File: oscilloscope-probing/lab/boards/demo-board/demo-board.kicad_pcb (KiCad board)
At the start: 4 copper layers, 12.8 x 6.5 mm, 265 parts, among them J1 CONN_01X03, J10 SMA-J-P-H-ST-EM1, J11 TESTCLIP, J12 TESTCLIP, J13 TESTCLIP, J14 USB_C_Receptacle_USB2.0, J15 TESTCLIP, J16 SMA-J-P-H-ST-EM1, J17 SMA-J-P-H-ST-EM1, J18 SMA-J-P-H-ST-EM1, J19 SMA-J-P-H-ST-EM1, J2 CORTEX_DEBUG_ETM, J3 XILINX_JTAG, J4 CORTEX_DEBUG_ETM, J5 DISPLAY, J6 CONN_01X06, J7 SMA-J-P-H-ST-EM1, J8 SMA-J-P-H-ST-EM1, J9 SMA-J-P-H-ST-EM1, Q1 SSM6N58NU, SW1 SWITCH, SW2 SWITCH, SW3 SWITCH, SW4 SWITCH, SW5 SWITCH, SW6 SWITCH, SW7 SWITCH, U1 FT234XD, U10 19-C47/RSGHBHC-5V01/2T, U11 19-C47/RSGHBHC-5V01/2T, U12 19-C47/RSGHBHC-5V01/2T, U13 19-C47/RSGHBHC-5V01/2T, U2 STM32L431-QFN48, U26 74LVC1T45, U3 LTC3374A, U39 NCP45525IMNTWG-H, U4 XC7A35T-2FGG484I, U5 STM32H750XBH6, U6 ECS-1612MV-250-CN, U7 ECS-1612MV-250-CN, U8 S25FL064LABMFI013, U9 SIT9121AI-2BF-XXS156.250000G

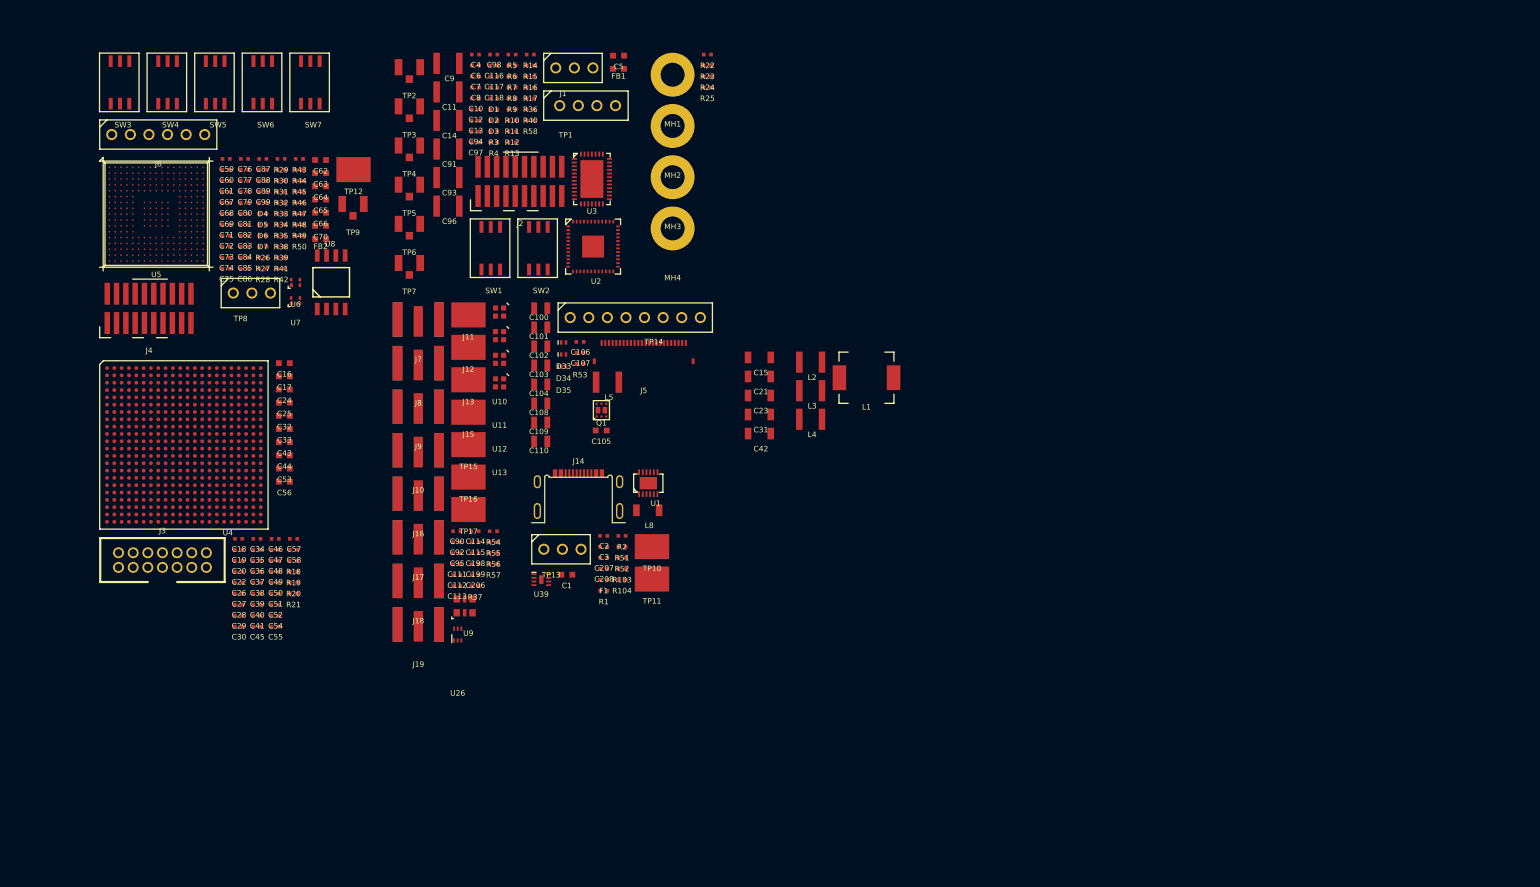
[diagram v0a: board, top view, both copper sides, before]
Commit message: Continued demo board layout
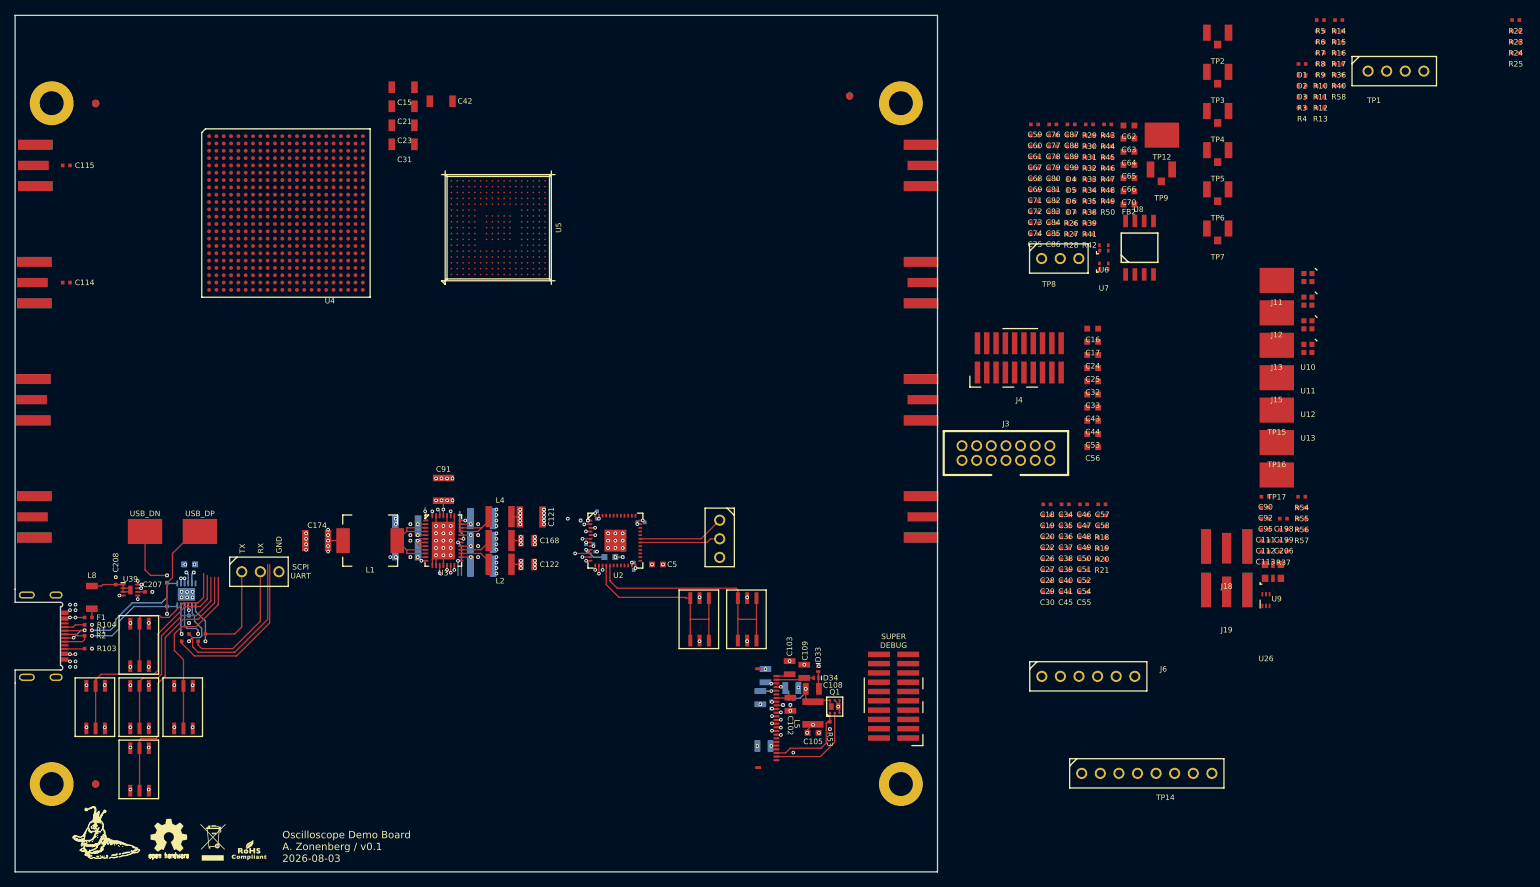
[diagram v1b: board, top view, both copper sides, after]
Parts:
- added C119: 0.47 uF, azonenberg_pcb:EIA_0402_CAP_NOSILK, F.Cu at (80.5, 98.0)
- added C120: 0.47 uF, azonenberg_pcb:EIA_0402_CAP_NOSILK, F.Cu at (80.5, 95.8)
- added C121: 47 uF, azonenberg_pcb:EIA_1210_CAP_NOSILK, F.Cu at (96.5, 92.5)
- added C122: 22 uF, azonenberg_pcb:EIA_0805_CAP_NOSILK, F.Cu at (96.0, 99.0)
- added C168: 22 uF, azonenberg_pcb:EIA_0805_CAP_NOSILK, F.Cu at (96.0, 95.8)
- added C174: 100 uF, azonenberg_pcb:EIA_1210_CAP_NOSILK, F.Cu at (67.2, 95.8)
- added FID1: FIDUCIAL, azonenberg_pcb:FIDUCIAL_1MM, B.Cu at (140.0, 35.0)
- added FID2: FIDUCIAL, azonenberg_pcb:FIDUCIAL_1MM, F.Cu at (140.0, 35.0)
- added FID3: FIDUCIAL, azonenberg_pcb:FIDUCIAL_1MM, B.Cu at (37.0, 36.0)
- added FID4: FIDUCIAL, azonenberg_pcb:FIDUCIAL_1MM, B.Cu at (37.0, 129.0)
- added FID5: FIDUCIAL, azonenberg_pcb:FIDUCIAL_1MM, F.Cu at (37.0, 36.1)
- added FID6: FIDUCIAL, azonenberg_pcb:FIDUCIAL_1MM, F.Cu at (37.0, 129.0)
- added J20: SMA-J-P-H-ST-EM1, azonenberg_pcb:CONN_SMA_EDGE_SAMTEC_SMA_J_P_H_ST_EM1, F.Cu at (26.3, 92.5)
- added J21: SMA-J-P-H-ST-EM1, azonenberg_pcb:CONN_SMA_EDGE_SAMTEC_SMA_J_P_H_ST_EM1, F.Cu at (26.1, 76.5)
- added M1: LOGO, azonenberg_pcb:LONGTHING-1200DPI, F.Cu at (39.0, 136.0)
- added M2: LOGO, w_logo:Logo_silk_ROHS_5x2.8mm, F.Cu at (58.0, 138.0)
- added M3: LOGO, w_logo:Logo_silk_WEEE_3.4x5mm, F.Cu at (53.0, 137.0)
- added M4: LOGO, w_logo:Logo_silk_OSHW_6x6mm, F.Cu at (47.0, 136.0)
- added R59: 0, azonenberg_pcb:EIA_0402_RES_NOSILK, F.Cu at (49.8, 109.0)
- added R60: 0, azonenberg_pcb:EIA_0402_RES_NOSILK, F.Cu at (52.0, 109.0)
- added R61: 0, azonenberg_pcb:EIA_0402_RES_NOSILK, F.Cu at (51.0, 109.0)
- added R62: 0, azonenberg_pcb:EIA_0402_RES_NOSILK, F.Cu at (48.8, 109.0)
- C1, C100, C101, C104, C106, C107, C11, C110, C116, C117, C118, C14, C2, C3, C4, C6, C7, C8, C9, C93, C96, D35, FB1, R51, R52, U1: moved to B.Cu
- moved J6 147.0 mm to (172.6, 114.3)
- moved MH2 123.6 mm to (31.0, 129.0)
- moved J4 119.1 mm to (163.2, 70.8)
- moved J3 116.1 mm to (161.3, 83.8)
- moved D1 110.5 mm to (201.8, 30.6)
- moved D2 110.5 mm to (201.8, 32.1)
- moved D3 110.5 mm to (201.8, 33.6)
- moved R10 110.5 mm to (204.3, 32.1)
- moved R11 110.5 mm to (204.3, 33.6)
- moved R12 110.5 mm to (204.3, 35.1)
- moved R13 110.5 mm to (204.3, 36.6)
- moved R14 110.5 mm to (206.8, 24.6)
- moved R15 110.5 mm to (206.8, 26.1)
- moved R16 110.5 mm to (206.8, 27.6)
- moved R17 110.5 mm to (206.8, 29.1)
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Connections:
- U1 pad 10: /USB power inlet and UART/UART_RX -> Net-(U1-RXD)
- U1 pad 11: /USB power inlet and UART/UART_CTS_N -> Net-(U1-CTS#)
- U1 pad 7: /USB power inlet and UART/UART_TX -> Net-(U1-TXD)
- U1 pad 8: /USB power inlet and UART/UART_RTS_N -> Net-(U1-RTS#)
- U2 pad 16: unconnected-(U2A-PA6-Pad16) -> /Power Supply/SOFT_PWR
- U2 pad 17: unconnected-(U2A-PA7-Pad17) -> /Power Supply/SOFT_RST
- U2 pad 18: /Power Supply/LTC_PGOOD_ALL -> unconnected-(U2B-PB0-Pad18)
- U2 pad 2: /Power Supply/SOFT_PWR -> /Power Supply/1V0_EN
- U2 pad 21: /Power Supply/1V2_EN -> /MCU/MCU_BOOT0
- U2 pad 22: /Power Supply/1V8_EN -> unconnected-(U2B-PB11-Pad22)
- U2 pad 25: /Power Supply/3V3_EN -> unconnected-(U2B-PB12-Pad25)
- U2 pad 3: /Power Supply/SOFT_RST -> /Power Supply/3V3_EN
- U2 pad 4: /FPGA support/FPGA_DONE -> /Power Supply/1V2_EN
- U2 pad 46: /Power Supply/1V0_EN -> /FPGA support/FPGA_DONE
- U2 pad 5: /MCU/MCU_BOOT0 -> /Power Supply/1V8_EN
- U2 pad 6: unconnected-(U2E-PH1-Pad6) -> /Power Supply/LTC_PGOOD_ALL
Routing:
- net /GND: track 0.00 -> 272.0 mm, vias 0 -> 110
- net /Power Supply/3V3_SB: track 0.00 -> 147.1 mm, vias 0 -> 14
- net /3V3: track 0.00 -> 127.4 mm, vias 0 -> 30
- net /VBUS: track 0.00 -> 105.3 mm, vias 0 -> 22
- net /MCU/DPAD_S: track 0.00 -> 35.7 mm
- net /Power Supply/SOFT_RST: track 0.00 -> 35.4 mm
- net /MCU/DPAD_W: track 0.00 -> 33.2 mm
- net /Power Supply/SOFT_PWR: track 0.00 -> 29.0 mm
- net /Power Supply/LTC_PGOOD_ALL: track 0.00 -> 27.7 mm, vias 0 -> 2
- net /Power Supply/LTC_VTEMP: track 0.00 -> 27.3 mm, vias 0 -> 3
- net /Power Supply/1V8_EN: track 0.00 -> 27.1 mm, vias 0 -> 2
- net /MCU/DPAD_SEL: track 0.00 -> 27.0 mm
- net /Power Supply/1V0_EN: track 0.00 -> 26.5 mm, vias 0 -> 2
- net /MCU/DPAD_E: track 0.00 -> 24.8 mm
- net /Power Supply/1V2_EN: track 0.00 -> 24.7 mm, vias 0 -> 2
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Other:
- board size 12.8 x 6.5 mm -> 126 x 117 mm
- copper layers 4 -> 8
- board text added: "Display body outline 59.20 x 29.20 mm"
- board text added: "GND"
- board text added: "North keepout for PnP rail 7 mm"
- board text added: "Oscilloscope Demo Board A. Zonenberg / v0.1 2026-08-03"
- board text added: "RX"
- board text added: "SCPI UART"
- board text added: "SUPER DEBUG"
- board text added: "South keepout for PnP rail 7 mm"
- board text added: "TX"
- board text added: "USB_DN"
- board text added: "USB_DP"
- board text added: "Visible area 48.548 x 23.712 mm"

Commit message: Continued demo board layout
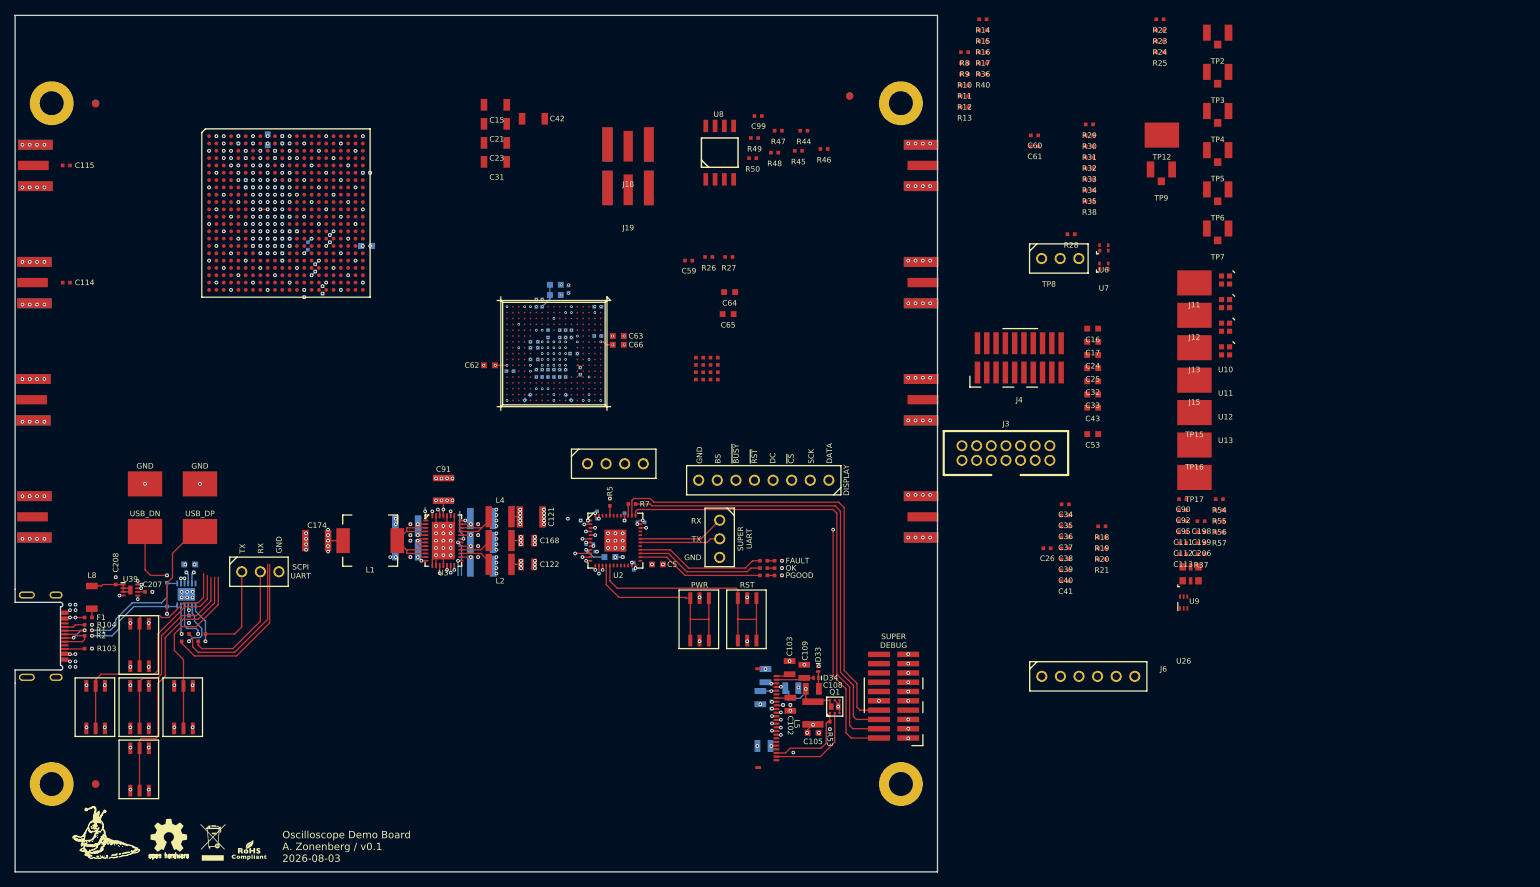
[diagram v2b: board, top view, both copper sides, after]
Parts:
- added C123: 0.47 uF, azonenberg_pcb:EIA_0402_CAP_NOSILK, B.Cu at (97.2, 63.3)
- added TP18: TESTCLIP, azonenberg_pcb:TESTPOINT_SMT_KEYSTONE_5016, F.Cu at (51.2, 88.0)
- added TP19: TESTCLIP, azonenberg_pcb:TESTPOINT_SMT_KEYSTONE_5016, F.Cu at (43.8, 88.0)
- C18, C19, C20, C22, C27, C28, C29, C30, C44, C45, C46, C47, C48, C49, C50, C51, C52, C54, C55, C56, C57, C58, C67, C68, C69, C70, C71, C72, C73, C74, C75, C76, C77, C78, C79, C80, C81, C82, C83, C84, C85, C86, C87, C88, C89, FB2, R6: moved to B.Cu
- moved C55 129.1 mm to (57.5, 43.0), turned to 90 degrees
- moved C57 128.0 mm to (56.5, 41.0), turned to 90 degrees
- moved C54 124.9 mm to (61.5, 43.0), turned to 90 degrees
- moved C58 123.1 mm to (62.5, 41.0), turned to 90 degrees
- moved C30 122.8 mm to (57.5, 47.0), turned to 90 degrees
- moved C56 120.3 mm to (60.5, 41.0), turned to 90 degrees
- moved TP1 119.4 mm to (108.0, 85.2)
- moved C22 118.1 mm to (59.0, 47.5), turned to 180 degrees
- moved R5 117.3 mm to (107.2, 90.5), turned to 90 degrees
- moved C51 117.0 mm to (62.5, 57.0), turned to -90 degrees
- moved C45 116.2 mm to (63.5, 55.0), turned to 90 degrees
- moved R6 115.9 mm to (109.2, 92.5), turned to -90 degrees
- moved C29 115.3 mm to (63.0, 51.5), turned to 180 degrees
- moved C20 114.7 mm to (62.0, 47.5)
- moved C28 114.3 mm to (62.0, 54.5), turned to 180 degrees
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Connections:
- net Net-(J2-TDO) renamed /Power Supply/SUPER_JTAG_TDOT
- R54 pad 2: Net-(U4E-IO_L1P_T0_AD0P_15) -> Net-(U4G-IO_L1P_T0_34)
- R55 pad 2: Net-(U4E-IO_L1N_T0_AD0N_15) -> Net-(U4G-IO_L1N_T0_34)
- R56 pad 2: Net-(U4E-IO_L2P_T0_AD8P_15) -> Net-(U4G-IO_L2P_T0_34)
- R57 pad 2: Net-(U4E-IO_L2N_T0_AD8N_15) -> Net-(U4G-IO_L2N_T0_34)
- TP14 pad 1: /MCU/DPY_DC -> /MCU/DPY_SPI_DATA
- TP14 pad 3: /MCU/DPY_SPI_DATA -> /MCU/DPY_SPI_CS_N
- TP14 pad 4: /MCU/DPY_RST_N -> /MCU/DPY_DC
- TP14 pad 5: /MCU/DPY_BS -> /MCU/DPY_RST_N
- TP14 pad 6: /MCU/DPY_SPI_CS_N -> /MCU/DPY_BUSY_N
- TP14 pad 7: /MCU/DPY_BUSY_N -> /MCU/DPY_BS
- U2 pad 21: /MCU/MCU_BOOT0 -> unconnected-(U2B-PB10-Pad21)
- U2 pad 33: unconnected-(U2A-PA12-Pad33) -> /MCU/MCU_BOOT0
- U4 pad G13: Net-(U4E-IO_L1N_T0_AD0N_15) -> unconnected-(U4E-IO_L1N_T0_AD0N_15-PadG13)
- U4 pad G15: Net-(U4E-IO_L2P_T0_AD8P_15) -> unconnected-(U4E-IO_L2P_T0_AD8P_15-PadG15)
- U4 pad G16: Net-(U4E-IO_L2N_T0_AD8N_15) -> unconnected-(U4E-IO_L2N_T0_AD8N_15-PadG16)
- U4 pad H13: Net-(U4E-IO_L1P_T0_AD0P_15) -> unconnected-(U4E-IO_L1P_T0_AD0P_15-PadH13)
- U4 pad T1: unconnected-(U4G-IO_L1P_T0_34-PadT1) -> Net-(U4G-IO_L1P_T0_34)
- U4 pad U1: unconnected-(U4G-IO_L1N_T0_34-PadU1) -> Net-(U4G-IO_L1N_T0_34)
- U4 pad U2: unconnected-(U4G-IO_L2P_T0_34-PadU2) -> Net-(U4G-IO_L2P_T0_34)
- U4 pad V2: unconnected-(U4G-IO_L2N_T0_34-PadV2) -> Net-(U4G-IO_L2N_T0_34)
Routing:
- net /GND: track 272.0 -> 796.0 mm, vias 110 -> 362
- net /3V3: track 127.4 -> 292.7 mm, vias 30 -> 90
- net /Power Supply/SUPER_JTAG_TDI: track 0.00 -> 62.9 mm
- net /Power Supply/SUPER_JTAG_TCK: track 0.00 -> 62.3 mm
- net /FPGA support/1V8: track 11.8 -> 72.7 mm, vias 4 -> 22
- net /Power Supply/SUPER_JTAG_TDOT: track 0.00 -> 60.8 mm
- net /Power Supply/SUPER_JTAG_TMS: track 0.00 -> 59.7 mm, vias 0 -> 2
- net /Power Supply/SUPER_RST_N: track 0.60 -> 56.4 mm, vias 1 -> 2
- net /FPGA support/1V0: track 6.15 -> 49.3 mm, vias 6 -> 28
- net /Power Supply/3V3_SB: track 147.1 -> 182.1 mm, vias 14 -> 15
- net /MCU/VCORE: track 0.00 -> 34.3 mm, vias 0 -> 5
- net /1V2: track 13.3 -> 40.0 mm, vias 4 -> 10
- net /MCU/DPY_SPI_SCK: track 10.1 -> 35.5 mm
- net /MCU/DPY_SPI_DATA: track 10.4 -> 35.6 mm
- net /MCU/DPY_SPI_CS_N: track 12.1 -> 37.0 mm
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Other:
- board text added: "BS"
- board text added: "DATA"
- board text added: "DC"
- board text added: "DISPLAY"
- board text added: "FAULT"
- board text added: "OK"
- board text added: "PGOOD"
- board text added: "PWR"
- board text added: "RST"
- board text added: "SCK"
- board text added: "SUPER UART"
- board text added: "~{BUSY}"
- board text added: "~{CS}"
- board text added: "~{RST}"

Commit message: Continued demo board layout
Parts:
- added D10: GREEN, azonenberg_pcb:EIA_0402_LED, F.Cu at (79.5, 58.5)
- added D11: GREEN, azonenberg_pcb:EIA_0402_LED, F.Cu at (79.5, 59.5)
- added D8: GREEN, azonenberg_pcb:EIA_0402_LED, F.Cu at (79.5, 56.5)
- added D9: GREEN, azonenberg_pcb:EIA_0402_LED, F.Cu at (79.5, 57.5)
- added R63: 33K, azonenberg_pcb:EIA_0402_RES_NOSILK, F.Cu at (77.5, 56.5)
- added R64: 33K, azonenberg_pcb:EIA_0402_RES_NOSILK, F.Cu at (77.5, 57.5)
- added R65: 33K, azonenberg_pcb:EIA_0402_RES_NOSILK, F.Cu at (77.5, 58.5)
- added R66: 33K, azonenberg_pcb:EIA_0402_RES_NOSILK, F.Cu at (77.5, 59.5)
- R14, R15, R16, R17, R34: moved to B.Cu
- moved R16 111.0 mm to (59.5, 78.2)
- moved R17 108.5 mm to (61.5, 78.2)
- moved R34 101.9 mm to (74.0, 71.5), turned to 180 degrees
- moved R14 100.8 mm to (61.5, 53.0), turned to 90 degrees
- moved R30 100.5 mm to (76.2, 68.5), turned to 180 degrees
- moved R31 100.5 mm to (76.2, 70.0), turned to 180 degrees
- moved R32 99.5 mm to (76.2, 67.8), turned to 180 degrees
- moved R33 99.5 mm to (76.2, 69.2), turned to 180 degrees
- moved R15 99.4 mm to (62.5, 53.0), turned to -90 degrees
- moved C18 15.0 mm to (59.0, 70.5)
- moved C19 15.0 mm to (62.0, 70.5)
- moved C20 15.0 mm to (62.0, 62.5)
- moved C22 15.0 mm to (59.0, 62.5)
- moved C27 15.0 mm to (64.0, 68.5)
- moved C28 15.0 mm to (62.0, 69.5)
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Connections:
- U4 pad B22: unconnected-(U4F-IO_L20N_T3_16-PadB22) -> /Test signals/FPGA_LED0
- U4 pad C22: unconnected-(U4F-IO_L20P_T3_16-PadC22) -> /Test signals/FPGA_LED1
- U4 pad D22: unconnected-(U4F-IO_L22N_T3_16-PadD22) -> /Test signals/FPGA_LED2
- U4 pad E22: unconnected-(U4F-IO_L22P_T3_16-PadE22) -> /Test signals/FPGA_LED3
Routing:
- net /3V3: track 292.7 -> 540.4 mm
- net /Power Supply/1V2_FB: track 2.40 -> 101.1 mm, vias 1 -> 4
- net /1V2: track 40.0 -> 112.0 mm, vias 10 -> 11
- net /GND: track 796.0 -> 827.9 mm, vias 362 -> 373
- net /FPGA support/1V0: track 49.3 -> 68.1 mm, vias 28 -> 29
- net /FPGA support/1V8: track 72.7 -> 87.8 mm, vias 22 -> 23
- net /MCU/FMC_A16: track 0.00 -> 8.42 mm
- net /MCU/FMC_AD9: track 0.00 -> 8.26 mm
- net /MCU/FMC_AD1: track 0.00 -> 7.65 mm
- net /MCU/FMC_AD12: track 0.00 -> 6.87 mm
- net /MCU/FMC_A17: track 0.00 -> 6.77 mm
- net /MCU/FMC_NOE: track 0.00 -> 6.21 mm
- net /MCU/FMC_AD5: track 0.00 -> 5.97 mm
- net /MCU/FMC_AD15: track 0.00 -> 5.97 mm
- net /MCU/FMC_AD10: track 0.00 -> 5.97 mm
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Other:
- board text added: "0"
- board text added: "1"
- board text added: "2"
- board text added: "3"
- board text added: "FPGA LED"
